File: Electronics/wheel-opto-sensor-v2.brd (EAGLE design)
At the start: 68.6 x 53.3 mm, 24 parts, among them IC1 BD6230F, IC2 BD6230F, IC3 TS5A23157

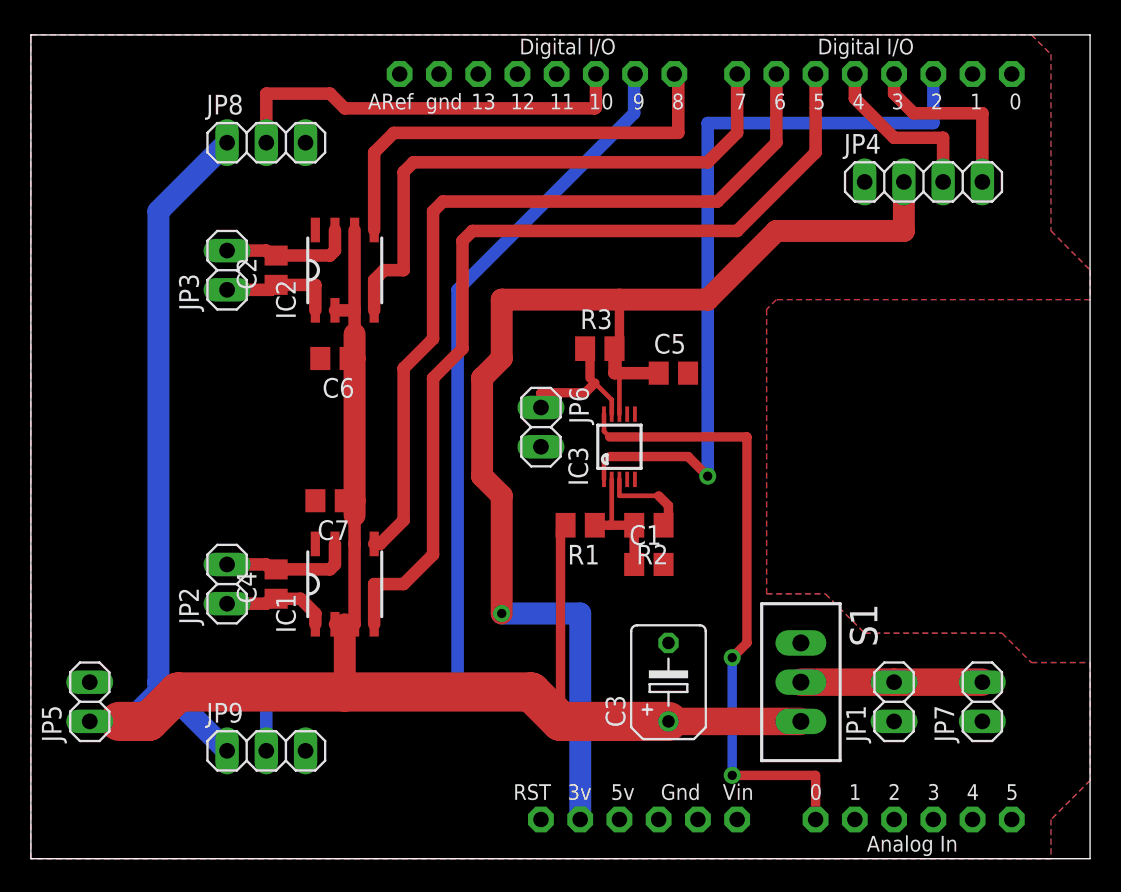
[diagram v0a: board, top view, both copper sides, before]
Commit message: Updated electronics to power the wheel sensors directly off the battery. (They take too much current from 3V3 if that is used; the sensors now have potential dividers so their output never exceeds 3v3.)
Added a PCB test program for the Wemos D1/ESP8266 board (W.I.P.)
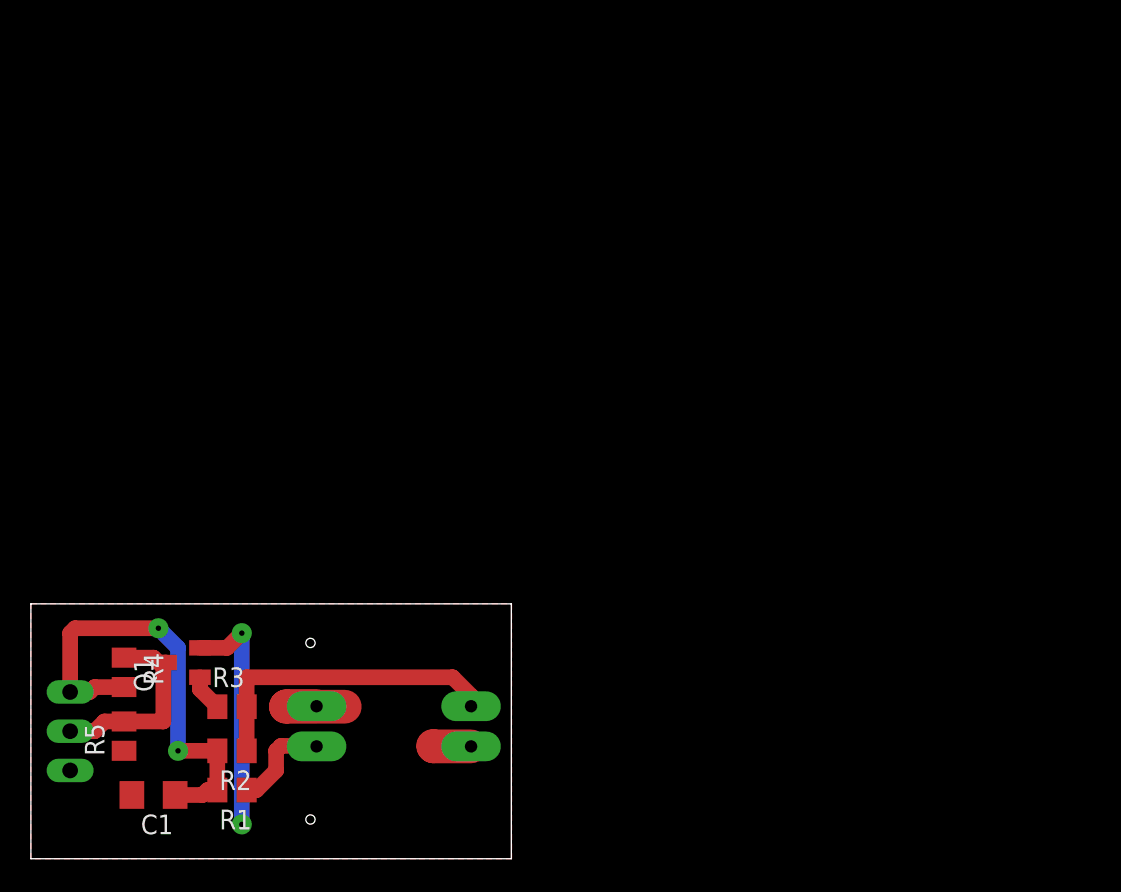
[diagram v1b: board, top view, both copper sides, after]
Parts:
- removed C2, C4, C5, C6, C7: 0.1uF, rcl:C0805
- removed C3: 1000uF, rcl:B45181B
- removed IC1, IC2: BD6230F, rohm:SOP8
- removed IC3: TS5A23157, reprapltd:MSOP10
- removed JP2, JP3, JP5, JP6, JP7: (no value), pinhead:1X02
- removed JP4: (no value), pinhead:1X04
- removed JP8, JP9: (no value), pinhead:1X03
- removed S1: TL36PO, switch:TL3XPO
- added Q1: (no value), adafruit:SOT23
- added R4: 1K2, rcl:M0805
- added R5: 1K, rcl:M0805
- C1: value 1uF -> 10uF; device rcl:C0805 -> rcl:C1206
- JP1: device pinhead:1X02 -> pinhead:1X03
- R1: value 15K -> 120R
- R2: value 10K -> 1K8
- R3: value 15K -> 10K
- U$1: value ARDUINO-BPLACE -> RPI-579N1; device adafruit:ARDUINO-BPLACE -> reprapltd:RPI-579N1
- moved JP1 53.4 mm to (2.54, 8.26), flipped to the bottom, turned to 270 degrees
- moved C1 35.4 mm to (7.94, 4.13), turned to 180 degrees
- moved R3 33.2 mm to (13.0, 9.84)
- moved R2 30.7 mm to (13.0, 6.99)
- moved R1 28.3 mm to (13.0, 4.45)
- moved U$1 25.0 mm to (23.5, 8.57), flipped to the bottom, turned to 180 degrees
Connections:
- removed net 5V: U$1.5V
- removed net N$10: IC2.5, U$1.D8
- removed net N$11: IC3.10, U$1.A0
- removed net N$12: C1.1, IC3.2, R1.1, R2.2
- removed net N$13: JP1.2, JP7.2, S1.2
- removed net N$14: IC3.9, JP6.1, R3.1
- removed net N$15: IC3.1, U$1.D2
- removed net N$17: JP9.2, U$1.D9
- removed net N$18: JP8.2, U$1.D10
- removed net N$4: C2.2, IC2.7, JP3.2
- removed net N$6: C4.2, IC1.7, JP2.2
- removed net N$7: IC1.5, U$1.D6
- removed net N$8: IC1.4, U$1.D5
- removed net N$9: IC2.4, U$1.D7
- removed net NC2: IC3.7
- removed net V+: C3.+, C6.1, C7.1, IC1.2, IC1.3, IC1.6, IC2.2, IC2.3, IC2.6, JP5.1, JP8.1, JP9.1, R1.2, S1.3
- removed net VIN: U$1.VIN
- net +3V3: now also C1.1, JP1.1, R1.2, R2.2, R4.2; no longer C5.1, IC3.8, JP4.2, R3.2, U$1.3V
- net GND: now also JP1.3, Q1.2, R5.1, U$1.P$2, U$1.P$4; no longer C3.-, C5.2, C6.2, C7.2, IC1.8, IC2.8, IC3.3, JP1.1, JP4.1, JP5.2, JP6.2, JP7.1, JP8.3, JP9.3, R2.1, U$1.GND, U$1.GND1, U$1.GND2
- net N$1: now also JP1.2, Q1.3, R4.1, R5.2; no longer JP4.4, U$1.D3
- net N$2: now also R1.1, U$1.P$1; no longer JP4.3, U$1.D4
- net N$3: now also Q1.1, R3.1; no longer C2.1, IC2.1, JP3.1
- net N$5: now also R2.1, R3.2, U$1.P$3; no longer C4.1, IC1.1, JP2.1
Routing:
- net V+: track 143.0 -> 0.00 mm
- net N$17: track 60.4 -> 0.00 mm
- net N$8: track 58.6 -> 0.00 mm
- net +3V3: track 83.2 -> 29.7 mm, vias 1 -> 2
- net N$7: track 51.8 -> 0.00 mm
- net N$15: track 49.1 -> 0.00 mm, vias 1 -> 0
- net N$11: track 41.1 -> 0.00 mm, vias 2 -> 0
- net N$9: track 36.9 -> 0.00 mm
- net N$10: track 29.1 -> 0.00 mm
- net N$18: track 27.1 -> 0.00 mm
- net GND: track 5.90 -> 23.8 mm, vias 0 -> 2
- net N$5: track 6.94 -> 20.5 mm
- net N$13: track 11.7 -> 0.00 mm
- net N$14: track 9.66 -> 0.00 mm
- net N$4: track 8.58 -> 0.00 mm
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- removed copper zone on layer 16, net GND
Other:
- board size 68.6 x 53.3 mm -> 31.1 x 16.5 mm
- board text removed: "+"
- board text removed: "+3V3"
- board text removed: "-"
- board text removed: "Batt"
- board text removed: "C"
- board text removed: "E"
- board text removed: "EPS8266/Arduino Shield V1.0 reprapltd.com Mechanics & software: Sally Bowyer Electronics: Adrian Bowyer Licence - GPL"
- board text removed: "Frank The Robot"
- board text removed: "G"
- board text removed: "L. sense"
- board text removed: "LIDAR"
- board text removed: "Left Motor"
- board text removed: "Pwr"
- board text removed: "R. sense"
- board text removed: "Right Motor"
- board text removed: "SCL"
- board text removed: "SDA"
- board text removed: "charge"
- board text removed: "photo"
- board text removed: "sig"
